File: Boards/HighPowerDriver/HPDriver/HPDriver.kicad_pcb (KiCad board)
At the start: 4 copper layers, 100.6 x 76.2 mm, 117 parts, among them J1 USB_B_Mini, J2 60V_In, J3 Coils, J4 Screw_Terminal_01x06, J5 AVR-ISP-6, Q1 IRFR5410, Q10 IRF4950S, Q11 BC817, Q12 BC817, Q13 BC817, Q14 BC817, Q2 IRFR3910, Q3 IRFR3910, Q4 IRFR5410, Q5 IRFR5410, Q6 IRFR3910, Q7 IRFR3910, Q8 IRFR5410, Q9 BC817, SW1 SW_Push, U1 LM5009MM, U10 ATtiny2313A-SU, U2 TMC262, U3 FT230XS, U4 SFH6156, U5 SFH6156, U6 TLP118, U7 LTV-827S, U8 LTV-827S, U9 74HC14, X1 16MHz, Y1 20MHz

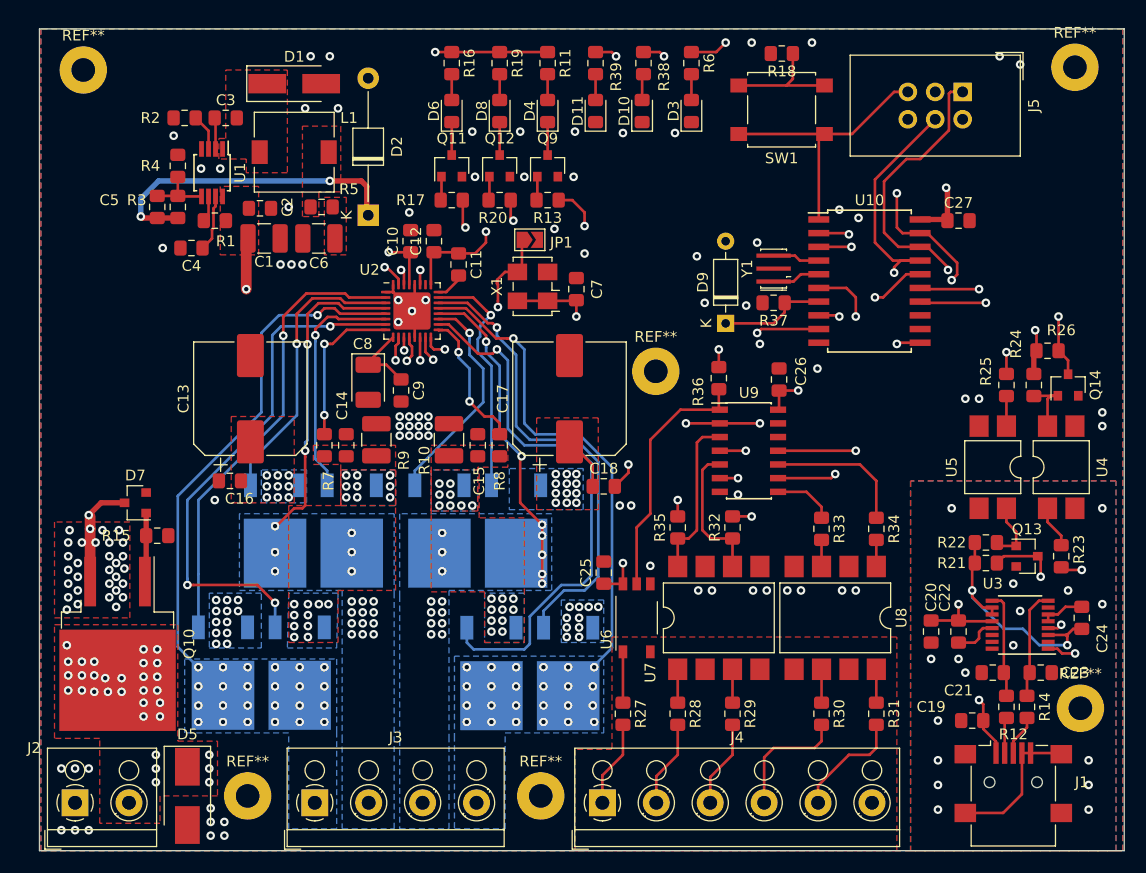
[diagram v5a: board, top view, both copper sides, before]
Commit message: Changed Connector to Phoenix Type
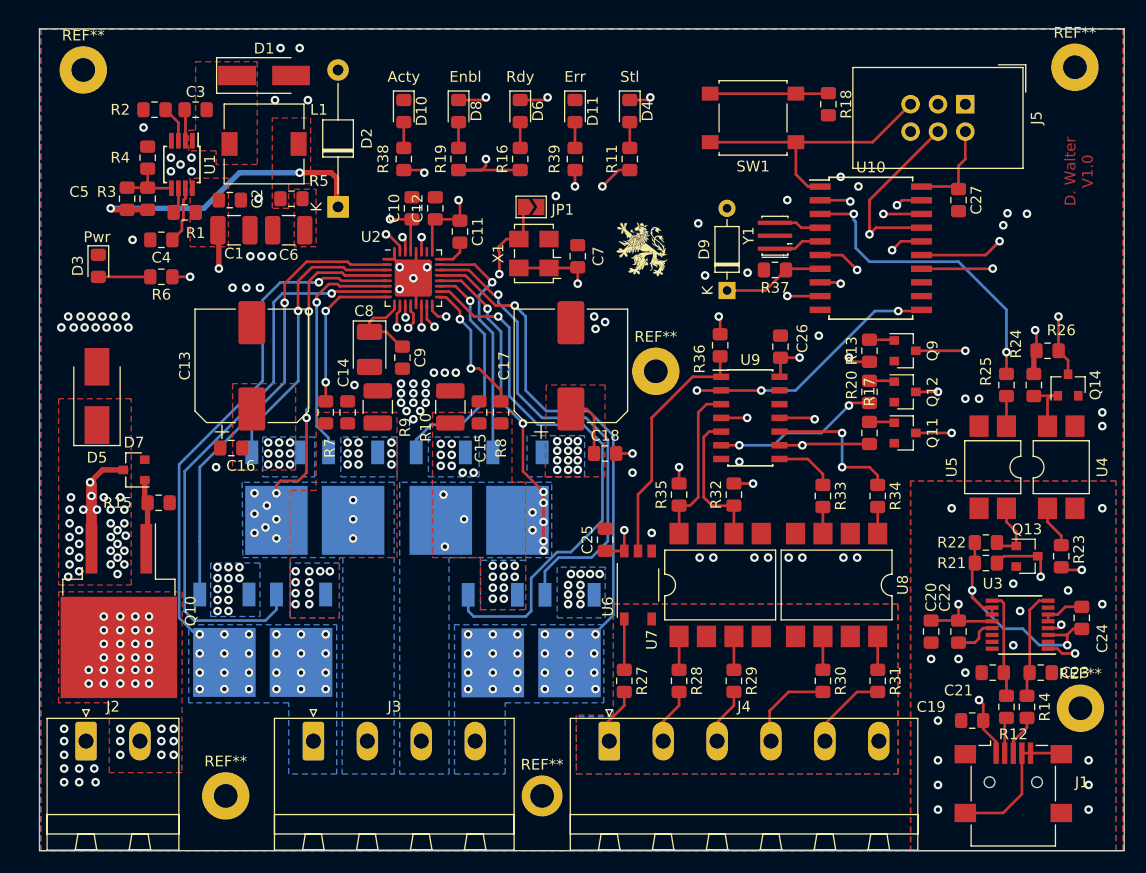
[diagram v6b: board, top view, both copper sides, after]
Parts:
- removed the REF** at (130.8, 135.9)
- removed the REF** at (103.6, 135.9)
- added G***: LOGO, Loewe:Loewe_Klein, F.Cu at (140.2, 85.2)
- added REF**: MountingHole_2.2mm_M2_ISO14580_Pad, MountingHole:MountingHole_2.2mm_M2_ISO14580_Pad, F.Cu at (130.9, 135.9)
- added REF**: MountingHole_2.2mm_M2_Pad, MountingHole:MountingHole_2.2mm_M2_Pad, F.Cu at (101.6, 135.9)
- J2: footprint TerminalBlock_RND:TerminalBlock_RND_205-00001_1x02_P5.00mm_Horizontal -> Connector_Phoenix_MSTB:PhoenixContact_MSTBA_2,5_2-G_1x02_P5.00mm_Horizontal
- J3: footprint TerminalBlock_RND:TerminalBlock_RND_205-00003_1x04_P5.00mm_Horizontal -> Connector_Phoenix_MSTB:PhoenixContact_MSTBA_2,5_4-G_1x04_P5.00mm_Horizontal
- J4: footprint TerminalBlock_RND:TerminalBlock_RND_205-00005_1x06_P5.00mm_Horizontal -> Connector_Phoenix_MSTB:PhoenixContact_MSTBA_2,5_6-G_1x06_P5.00mm_Horizontal
- moved D3 56.8 mm to (89.8, 86.7), turned to 270 degrees
- moved R6 53.0 mm to (95.6, 87.8), turned to 180 degrees
- moved Q11 48.8 mm to (164.6, 102.2), turned to 0 degrees
- moved R17 44.3 mm to (161.3, 102.2), turned to 90 degrees
- moved Q12 43.0 mm to (164.6, 98.4), turned to 0 degrees
- moved R20 38.6 mm to (161.3, 98.4), turned to 90 degrees
- moved D5 38.0 mm to (89.7, 98.8), turned to 90 degrees
- moved Q9 37.3 mm to (164.6, 94.6), turned to 0 degrees
- moved R13 33.0 mm to (161.3, 94.6), turned to 90 degrees
- moved R38 23.9 mm to (118.1, 76.8), turned to 90 degrees
- moved D10 22.1 mm to (118.1, 72.4), turned to 270 degrees
- moved R11 11.7 mm to (139.1, 76.8), turned to 90 degrees
- moved R16 10.9 mm to (128.9, 76.8), turned to 90 degrees
- moved R19 9.67 mm to (123.2, 76.8), turned to 90 degrees
- moved R39 9.09 mm to (134.0, 76.8), turned to 90 degrees
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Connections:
- D5 pad 1: Net-(D5-Pad1) -> +48V
- J2 pad 2: Net-(D5-Pad1) -> Net-(J2-Pad2)
- Q10 pad 2: Net-(D5-Pad1) -> Net-(J2-Pad2)
- U10 pad 12: (no net) -> Net-(U10-Pad12)
- U10 pad 13: (no net) -> Net-(U10-Pad13)
- U2 pad 26: (no net) -> Net-(U2-Pad26)
- U3 pad 14: (no net) -> Net-(U3-Pad14)
- U3 pad 15: (no net) -> Net-(U3-Pad15)
- U3 pad 16: (no net) -> Net-(U3-Pad16)
- U3 pad 2: (no net) -> Net-(U3-Pad2)
- U3 pad 7: (no net) -> Net-(U3-Pad7)
- U9 pad 12: (no net) -> Net-(U9-Pad12)
- U9 pad 13: (no net) -> Net-(U9-Pad13)
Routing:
- net Net-(D6-Pad1): track 3.05 -> 76.5 mm, vias 0 -> 3
- net Net-(D8-Pad1): track 3.05 -> 76.3 mm, vias 0 -> 3
- net Net-(D4-Pad1): track 3.05 -> 61.1 mm, vias 0 -> 3
- net /Connector/Ready: track 70.1 -> 36.7 mm, vias 4 -> 3
- net +48V: track 98.7 -> 80.6 mm
- net /Connector/Error: track 69.4 -> 52.7 mm, vias 3 -> 2
- net /Controller/SCK: track 79.1 -> 67.7 mm, vias 3 -> 2
- net /Controller/MISO: track 79.7 -> 69.3 mm
- net /Connector/Stall: track 87.3 -> 77.3 mm, vias 6 -> 5
- net /Driver/DriveEN: track 79.2 -> 71.3 mm
- net /Controller/MOSI: track 74.4 -> 67.7 mm
- net /Connector/Step: track 77.9 -> 72.3 mm, vias 6 -> 5
- net /Connector/Active: track 61.1 -> 66.6 mm, vias 3 -> 2
- net Net-(Q6-Pad1): track 48.4 -> 53.7 mm, vias 3 -> 1
- net Net-(J4-Pad4): track 11.7 -> 8.47 mm
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- added copper zone on B.Cu, net GNDA
- added copper zone on In1.Cu, net GNDA
- added copper zone on In2.Cu, net GNDA
- added copper zone on F.Cu, net Net-(J2-Pad2)
- added copper zone on In1.Cu, net Net-(J2-Pad2)
- removed copper zone on F.Cu, net Net-(D5-Pad1)
- removed copper zone on In1.Cu, net Net-(D5-Pad1)
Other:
- board text added: "Acty"
- board text added: "D. Walter V1.0"
- board text added: "Enbl"
- board text added: "Err"
- board text added: "Pwr"
- board text added: "Rdy"
- board text added: "Stl"

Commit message: Minor Layout changes
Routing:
- net Net-(Q4-Pad1): track 45.0 -> 43.5 mm
- net /Connector/Rx: track 34.6 -> 33.7 mm
- net Net-(Q7-Pad1): track 22.3 -> 23.1 mm
- net /Connector/Step: track 72.3 -> 71.7 mm
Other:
- board text added: "Act."
- board text added: "Enbl."
- board text added: "Error"
- board text added: "Ready"
- board text added: "Reset"
- board text added: "Stall"
- board text removed: "Acty"
- board text removed: "Enbl"
- board text removed: "Err"
- board text removed: "Rdy"
- board text removed: "Stl"

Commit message: Release 1.0
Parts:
- moved C27 0.76 mm to (168.8, 80.6)
- moved R27 0.64 mm to (139.2, 125.2)
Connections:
- REF** pad 1: (no net) -> GND (x5)
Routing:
- net /Connector/Ready: track 36.7 -> 26.8 mm, vias 3 -> 2
- net /Connector/Coil_B1: track 30.2 -> 24.7 mm, vias 12 -> 14
- net Net-(Q3-Pad1): track 51.0 -> 49.5 mm
- net Net-(Q4-Pad1): track 43.5 -> 42.2 mm
- net /Driver/DriveEN: track 71.6 -> 70.8 mm
- net /Controller/MISO: track 69.5 -> 68.7 mm
- net Net-(Q7-Pad1): track 23.1 -> 23.7 mm
- net Net-(D6-Pad1): track 76.5 -> 76.0 mm
- net Net-(J4-Pad4): track 8.47 -> 7.95 mm
- net Net-(D8-Pad1): track 76.3 -> 75.8 mm
- net Net-(J2-Pad2): vias 35 -> 41
- net GNDS: vias 17 -> 26
- net GNDA: vias 0 -> 20
- net GND: vias 83 -> 178
- net /Connector/Coil_A2: vias 13 -> 14
